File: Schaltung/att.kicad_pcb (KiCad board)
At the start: 2 copper layers, 80 x 80 mm, 45 parts, among them J1 12V Power supply, J2 R&S Attenuator 26.5 GHz, J3 dB Drehgeber, J4 ESP-Controller, J6 Display, U1 DRV8871DDA, U2 DRV8871DDA, U3 DRV8871DDA, U4 DRV8871DDA, U5 DRV8871DDA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

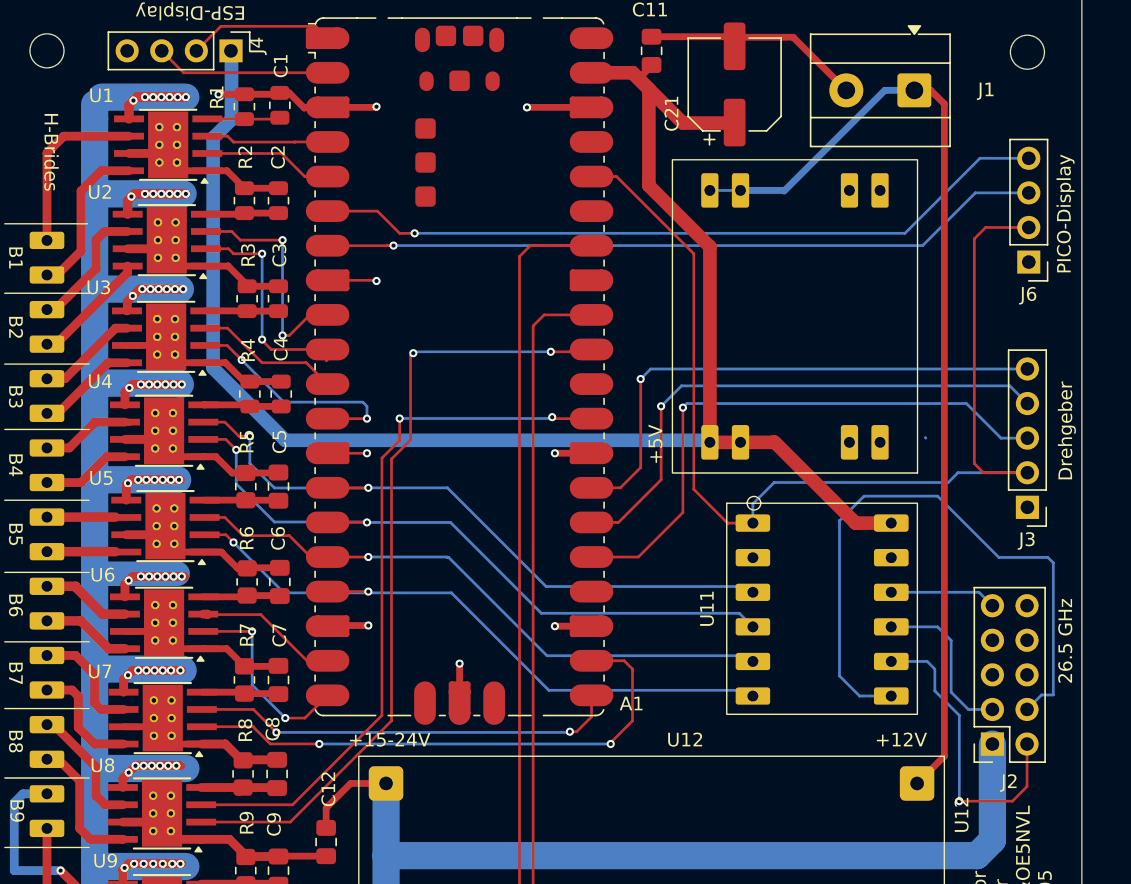
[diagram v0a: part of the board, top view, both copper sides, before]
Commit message: vor 26.5 ghz buchse ändern
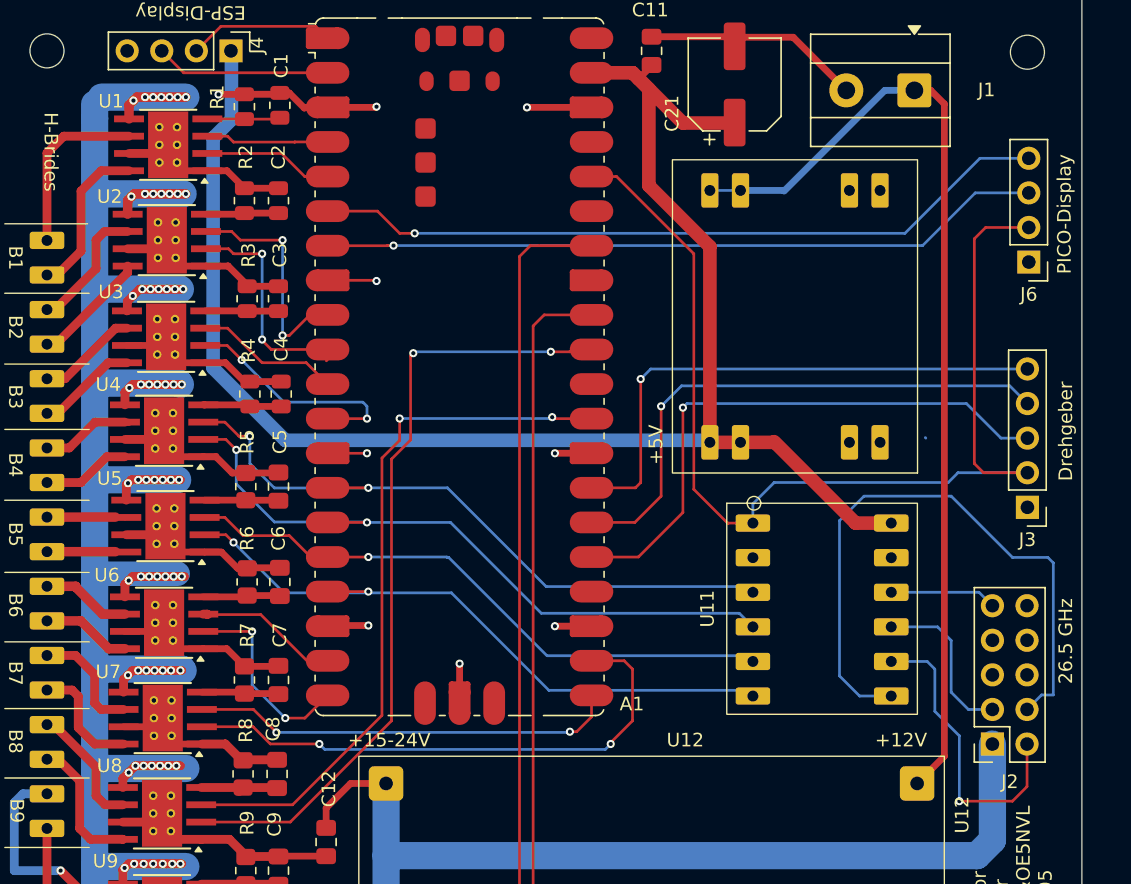
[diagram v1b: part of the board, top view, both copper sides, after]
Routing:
- net /D_DT: track 39.9 -> 40.6 mm
- net /d_CLK: track 39.0 -> 39.7 mm
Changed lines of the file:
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@@
 		(tags "HTSOP 1.27")
 		(property "Reference" "U7"
-			(at 4.6 3.4 0)
+			(at 4 3.4 0)
 			(layer "F.SilkS")
 			(effects
@@
 		(tags "HTSOP 1.27")
 		(property "Reference" "U3"
-			(at 4.95 3.6 0)
+			(at 4.05 3.3 0)
 			(layer "F.SilkS")
 			(effects
@@
 		(tags "HTSOP 1.27")
 		(property "Reference" "U6"
-			(at 4.5 3.5 0)
+			(at 4.2 3.5 0)
 			(layer "F.SilkS")
 			(effects
@@
 		(tags "HTSOP 1.27")
 		(property "Reference" "U1"
-			(at 4.9 3.6 0)
+			(at 4.2 3.2 0)
 			(layer "F.SilkS")
 			(effects
@@
 		(tags "HTSOP 1.27")
 		(property "Reference" "U5"
-			(at 4.7 3.5 0)
+			(at 4.1 3.5 0)
 			(layer "F.SilkS")
 			(effects
@@
 		(tags "HTSOP 1.27")
 		(property "Reference" "U8"
-			(at 4.35 3.5 0)
+			(at 3.85 3.5 0)
 			(layer "F.SilkS")
 			(effects
@@
 		(tags "HTSOP 1.27")
 		(property "Reference" "U4"
-			(at 4.7 3.6 0)
+			(at 4.1 3.4 0)
 			(layer "F.SilkS")
 			(effects
@@
 		(tags "HTSOP 1.27")
 		(property "Reference" "U2"
-			(at 4.9 3.5 0)
+			(at 4.2 3.2 0)
 			(layer "F.SilkS")
 			(effects
@@
 	)
 	(segment
-		(start 76.6 102.5)
-		(end 73 102.5)
+		(start 99.6 97)
+		(end 98.99 96.39)
 		(width 0.2)
 		(layer "F.Cu")
@@
 	)
 	(segment
-		(start 99.6 97)
-		(end 98.99 96.39)
+		(start 97.9 102.5)
+		(end 99.6 100.8)
 		(width 0.2)
 		(layer "F.Cu")
@@
 	)
 	(segment
-		(start 97.9 102.5)
-		(end 99.6 100.8)
+		(start 71.735 101.235)
+		(end 67.975 101.235)
 		(width 0.2)
 		(layer "F.Cu")
@@
 	)
 	(segment
-		(start 99.6 100.8)
-		(end 99.6 97)
+		(start 76.6 102.5)
+		(end 73 102.5)
 		(width 0.2)
 		(layer "F.Cu")
@@
 	)
 	(segment
-		(start 71.735 101.235)
-		(end 67.975 101.235)
+		(start 99.6 100.8)
+		(end 99.6 97)
 		(width 0.2)
 		(layer "F.Cu")
@@
 	(segment
 		(start 76.6 102.5)
+		(end 77 102.9)
+		(width 0.2)
+		(layer "B.Cu")
+		(net "Net-(A1-GPIO17)")
+	)
+	(segment
+		(start 77 102.9)
+		(end 97.6 102.9)
+		(width 0.2)
+		(layer "B.Cu")
+		(net "Net-(A1-GPIO17)")
+	)
+	(segment
+		(start 97.6 102.9)
 		(end 98 102.5)
 		(width 0.2)
@@
 	)
 	(segment
-		(start 98.57 86.23)
-		(end 101.7 83.1)
+		(start 101.7 84.3)
+		(end 101.7 77.7)
 		(width 0.2)
 		(layer "F.Cu")
@@
 	)
 	(segment
-		(start 96.59 86.23)
-		(end 98.57 86.23)
+		(start 99.77 86.23)
+		(end 101.7 84.3)
 		(width 0.2)
 		(layer "F.Cu")
@@
 	)
 	(segment
-		(start 101.7 83.1)
-		(end 101.7 77.7)
+		(start 96.59 86.23)
+		(end 99.77 86.23)
 		(width 0.2)
 		(layer "F.Cu")
@@
 	)
 	(segment
-		(start 98.71 83.69)
-		(end 96.59 83.69)
+		(start 100.2 75.7)
+		(end 100.2 83.3)
 		(width 0.2)
 		(layer "F.Cu")
@@
 	)
 	(segment
-		(start 100.2 82.2)
-		(end 98.71 83.69)
+		(start 100.2 83.3)
+		(end 99.81 83.69)
 		(width 0.2)
 		(layer "F.Cu")
@@
 	)
 	(segment
-		(start 100.2 75.7)
-		(end 100.2 82.2)
+		(start 99.81 83.69)
+		(end 96.59 83.69)
 		(width 0.2)
 		(layer "F.Cu")
@@
 	)
 	(segment
-		(start 121.8 98.6)
-		(end 121.8 97)
+		(start 121.24 96.44)
+		(end 118.6 96.44)
 		(width 0.2)
 		(layer "B.Cu")
@@
 	)
 	(segment
-		(start 123.6 100.4)
-		(end 121.8 98.6)
+		(start 123.6 106.7)
+		(end 123.6 101.9)
 		(width 0.2)
 		(layer "B.Cu")
@@
 	)
 	(segment
-		(start 121.8 97)
-		(end 121.24 96.44)
+		(start 123.6 101.9)
+		(end 121.8 100.1)
 		(width 0.2)
 		(layer "B.Cu")
@@
 	)
 	(segment
-		(start 123.6 106.7)
-		(end 123.6 100.4)
+		(start 121.8 100.1)
+		(end 121.8 97)
 		(width 0.2)
 		(layer "B.Cu")
@@
 	)
 	(segment
-		(start 121.24 96.44)
-		(end 118.6 96.44)
+		(start 121.8 97)
+		(end 121.24 96.44)
 		(width 0.2)
 		(layer "B.Cu")
@@
 	)
 	(segment
-		(start 129.635 98.9)
-		(end 128.57 99.965)
+		(start 130.5 89.2)
+		(end 130.5 98.9)
 		(width 0.2)
 		(layer "B.Cu")
@@
 	)
 	(segment
-		(start 114.8 97.5)
-		(end 114.8 86.1)
+		(start 130.5 98.9)
+		(end 129.635 98.9)
 		(width 0.2)
 		(layer "B.Cu")
@@
 	)
 	(segment
-		(start 116.28 98.98)
-		(end 114.8 97.5)
+		(start 114.8 86.1)
+		(end 116.6 84.3)
 		(width 0.2)
 		(layer "B.Cu")
@@
 	)
 	(segment
-		(start 122 84.3)
-		(end 126.5 88.8)
+		(start 114.8 97.5)
+		(end 114.8 86.1)
 		(width 0.2)
 		(layer "B.Cu")
@@
 	)
 	(segment
-		(start 130.5 98.9)
-		(end 129.635 98.9)
+		(start 116.6 84.3)
+		(end 123 84.3)
 		(width 0.2)
 		(layer "B.Cu")
@@
 	)
 	(segment
-		(start 126.5 88.8)
-		(end 130.1 88.8)
+		(start 116.28 98.98)
+		(end 114.8 97.5)
 		(width 0.2)
 		(layer "B.Cu")
@@
 	)
 	(segment
-		(start 114.8 86.1)
-		(end 116.6 84.3)
+		(start 129.635 98.9)
+		(end 128.57 99.965)
 		(width 0.2)
 		(layer "B.Cu")
@@
 	)
 	(segment
-		(start 116.6 84.3)
-		(end 122 84.3)
+		(start 123 84.3)
+		(end 127.5 88.8)
 		(width 0.2)
 		(layer "B.Cu")
@@
 	)
 	(segment
-		(start 130.5 89.2)
-		(end 130.5 98.9)
+		(start 127.5 88.8)
+		(end 130.1 88.8)
 		(width 0.2)
 		(layer "B.Cu")

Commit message: produktion
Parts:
- added J5: ATT_SEL, Connector_PinSocket_2.54mm:PinSocket_2x02_P2.54mm_Vertical, F.Cu at (127.5, 62.5)
- J2: footprint Connector_PinSocket_2.54mm:PinSocket_2x05_P2.54mm_Vertical -> Connector_PinHeader_2.54mm:PinHeader_2x05_P2.54mm_Vertical
- moved C12 17.0 mm to (65.8, 122.4)
- moved J2 13.1 mm to (128.7, 115.3)
- moved J3 11.4 mm to (128.6, 96.5)
- moved J6 10.7 mm to (128.7, 77.8)
- moved U12 3.03 mm to (98.0, 114.8)
- moved U11 1.95 mm to (111.6, 88.5)
- moved C10 1.46 mm to (72.1, 120.9), turned to -90 degrees
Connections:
- J2 pad 1: +15V-24V -> /40dBa
- J2 pad 10: unconnected-(J2-Pin_5-Pad10) -> /10dB
- J2 pad 2: /40dBa -> +15V-24V
- J2 pad 3: /20dB -> /40dBb
- J2 pad 4: /40dBb -> /20dB
- J2 pad 9: /10dB -> unconnected-(J2-Pin_5-Pad9)
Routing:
- net Net-(A1-GPIO3): track 9.59 -> 62.8 mm, vias 0 -> 1
- net Net-(A1-GPIO2): track 9.02 -> 60.2 mm, vias 0 -> 1
- net /40dBa: track 22.4 -> 41.4 mm, vias 1 -> 0
- net /40dBb: track 46.4 -> 30.0 mm
- net /20dB: track 12.2 -> 26.7 mm, vias 0 -> 1
- net /10dB: track 7.84 -> 21.5 mm, vias 0 -> 2
- net /D_SW: track 42.2 -> 54.4 mm
- net /D_DT: track 40.6 -> 52.6 mm
- net +15V-24V: track 269.0 -> 257.0 mm, vias 69 -> 63
- net /d_CLK: track 39.7 -> 51.0 mm
- net Net-(A1-GPIO26_ADC0): track 57.9 -> 63.7 mm
- net Net-(A1-GPIO22): track 52.5 -> 57.7 mm
- net Net-(J1-Pin_1): track 72.0 -> 77.1 mm
- net +3.3V: track 80.1 -> 82.8 mm, vias 0 -> 1
- net GND: track 161.7 -> 159.1 mm, vias 9 -> 14
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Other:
- board text removed: "Attenuator Controller OE5RNL&OE5NVL V1 202505"

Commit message: production-files
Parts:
- J5: footprint Connector_PinSocket_2.54mm:PinSocket_2x02_P2.54mm_Vertical -> Connector_PinHeader_2.54mm:PinHeader_2x02_P2.54mm_Vertical
- moved J5 2.87 mm to (126.4, 59.8), turned to 0 degrees
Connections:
- J5 pad 1: Net-(A1-GPIO3) -> Net-(A1-GPIO2)
- J5 pad 3: Net-(A1-GPIO2) -> Net-(A1-GPIO3)
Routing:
- net Net-(A1-GPIO3): track 62.8 -> 60.8 mm
- net Net-(A1-GPIO2): track 60.2 -> 59.0 mm
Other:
- board text added: "OE5RNL&OE5NVL Attenuator-Controller V1.0 202604 ADL516"

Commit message: final vor nvl check
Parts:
- C10: footprint Capacitor_SMD:CP_Elec_6.3x5.2 -> Capacitor_THT:CP_Radial_D8.0mm_P5.00mm
- moved C10 1.84 mm to (71.2, 119.3)
- moved C12 1.30 mm to (64.5, 122.4)
- moved J4 0.89 mm to (71.0, 51.6)
- moved H2 0.10 mm to (128.6, 51.6)
- moved H3 0.10 mm to (56.6, 123.6)
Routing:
- net +15V-24V: track 257.0 -> 250.6 mm, vias 63 -> 66
- net GND: track 159.1 -> 154.1 mm, vias 14 -> 12
- net Net-(A1-GPIO28_ADC2): track 75.0 -> 77.1 mm
- net Net-(A1-GPIO27_ADC1): track 68.8 -> 69.9 mm
- net /Disp_SCL: track 55.1 -> 54.3 mm
- net Net-(U13B-B2b): track 8.58 -> 9.28 mm
- net Net-(U13B-B2a): track 9.53 -> 10.2 mm
- net Net-(A1-GPIO9): track 17.5 -> 18.1 mm
- net Net-(U13C-B3b): track 7.41 -> 7.95 mm

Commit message: nvl
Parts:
- added C1: 100nF, Capacitor_SMD:C_0805_2012Metric_Pad1.18x1.45mm_HandSolder, F.Cu at (43.5, 61.0)
- added C2: 100nF, Capacitor_SMD:C_0805_2012Metric_Pad1.18x1.45mm_HandSolder, F.Cu at (43.5, 64.0)
- added C3: 100nF, Capacitor_SMD:C_0805_2012Metric_Pad1.18x1.45mm_HandSolder, F.Cu at (43.5, 67.0)
- added C4: 100nF, Capacitor_SMD:C_0805_2012Metric_Pad1.18x1.45mm_HandSolder, F.Cu at (43.5, 70.0)
- moved C11 0.92 mm to (101.9, 51.8)
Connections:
- C11 pad 2: +5V -> Net-(J1-Pin_1)
- C21 pad 1: +5V -> Net-(J1-Pin_1)
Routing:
- net +5V: track 120.1 -> 108.9 mm
- net Net-(J1-Pin_1): track 77.1 -> 85.1 mm
- net GND: track 154.1 -> 152.9 mm

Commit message: att select
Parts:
- removed J5: ATT_SEL, Connector_PinHeader_2.54mm:PinHeader_2x02_P2.54mm_Vertical
- added C13: 100nF, Capacitor_SMD:C_0805_2012Metric_Pad1.18x1.45mm_HandSolder, F.Cu at (100.8, 72.4)
- added R10: 15k, Resistor_SMD:R_0805_2012Metric_Pad1.20x1.40mm_HandSolder, F.Cu at (128.8, 61.4)
- added R11: 15k, Resistor_SMD:R_0805_2012Metric_Pad1.20x1.40mm_HandSolder, F.Cu at (128.8, 64.8)
- moved C1 77.0 mm to (104.8, 107.7)
- moved C2 77.0 mm to (104.8, 110.7)
- moved C4 77.0 mm to (104.8, 116.7)
- moved C3 76.9 mm to (104.6, 113.7), turned to 180 degrees
- moved C11 1.04 mm to (100.9, 51.5)
- moved U12 0.14 mm to (97.9, 114.7)
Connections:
- A1 pad 24: unconnected-(A1-GPIO18-Pad24) -> Net-(A1-GPIO18)
- U8 pad 2: Net-(A1-GPIO26_ADC0) -> Net-(A1-GPIO22)
- U8 pad 3: Net-(A1-GPIO22) -> Net-(A1-GPIO18)
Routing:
- net Net-(A1-GPIO18): track 0.00 -> 53.2 mm, vias 0 -> 2
- net Net-(A1-GPIO3): track 60.8 -> 9.59 mm, vias 1 -> 0
- net Net-(A1-GPIO2): track 59.0 -> 9.02 mm, vias 1 -> 0
- net +3.3V: track 82.8 -> 99.2 mm
- net Net-(A1-GPIO26_ADC0): track 63.3 -> 48.5 mm
- net GND: track 152.9 -> 158.7 mm, vias 12 -> 14
- net Net-(J1-Pin_1): track 85.1 -> 86.8 mm

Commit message: vor produktion 1
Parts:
- removed the C1 at (104.8, 107.7)
- removed the C1 at (73.7, 55.6)
- removed the C2 at (104.8, 110.7)
- removed the C2 at (73.6, 62.6)
- removed the C3 at (104.6, 113.7)
- removed the C3 at (73.6, 69.8)
- removed the C4 at (73.8, 76.8)
- removed the C4 at (104.8, 116.7)
- added C1: 100nF, Capacitor_SMD:C_0805_2012Metric, F.Cu at (73.7, 55.7)
- added C2: 100nF, Capacitor_SMD:C_0805_2012Metric, F.Cu at (73.7, 62.6)
- added C3: 100nF, Capacitor_SMD:C_0805_2012Metric, F.Cu at (73.7, 69.8)
- added C4: 100nF, Capacitor_SMD:C_0805_2012Metric, F.Cu at (73.7, 76.8)
- C11, C12, C13, C5, C6, C7, C8, C9: footprint Capacitor_SMD:C_0805_2012Metric_Pad1.18x1.45mm_HandSolder -> Capacitor_SMD:C_0805_2012Metric
- R10, R11, R5, R6, R7, R8, R9: footprint Resistor_SMD:R_0805_2012Metric_Pad1.20x1.40mm_HandSolder -> Resistor_SMD:R_0805_2012Metric
- moved R10 2.40 mm to (128.7, 59.0)
- moved R11 2.30 mm to (128.7, 62.5)
- moved R4 0.50 mm to (71.0, 76.8)
- moved R6 0.35 mm to (71.0, 90.8)
- moved R3 0.30 mm to (71.0, 69.8)
- moved R9 0.22 mm to (71.0, 111.9)
- moved C8 0.21 mm to (73.7, 104.8)
- moved C11 0.20 mm to (101.1, 51.5)
- moved C6 0.15 mm to (73.7, 90.8)
- moved C12 0.15 mm to (64.5, 122.5)
- moved R5 0.13 mm to (71.1, 83.7)
- moved R7 0.13 mm to (71.0, 97.9)
- moved C5 0.11 mm to (73.7, 83.7)
- moved C7 0.11 mm to (73.7, 97.8)
- moved C9 0.11 mm to (73.7, 111.8)
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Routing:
- net +3.3V: track 99.2 -> 102.4 mm
- net Net-(A1-GPIO26_ADC0): track 48.5 -> 50.6 mm
- net GND: track 158.7 -> 157.0 mm
- net Net-(J1-Pin_1): track 86.8 -> 85.9 mm
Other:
- board text added: "ATT-Select"

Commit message: produktion-version
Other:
- board text added: "+ 12V -"
